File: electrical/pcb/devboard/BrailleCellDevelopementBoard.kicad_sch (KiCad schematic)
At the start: 3 parts, among them J2 USB_C_Receptacle_USB2.0_14P, Q3 PMOS

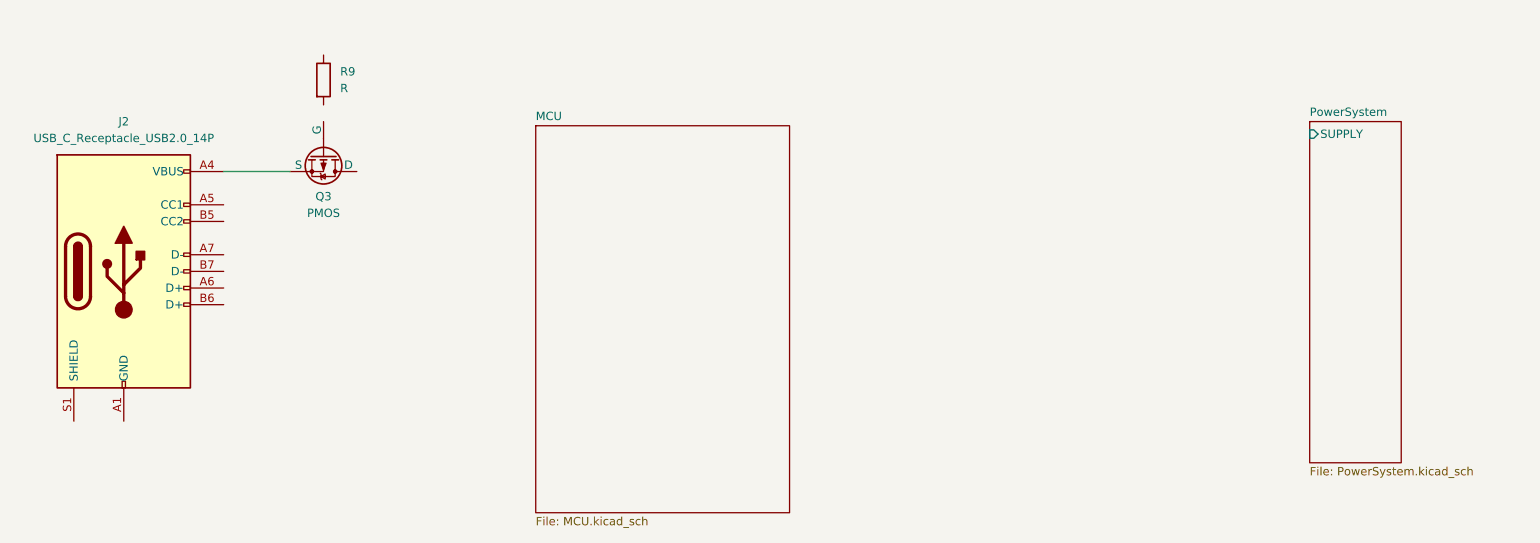
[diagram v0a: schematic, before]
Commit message: cell shifter routed
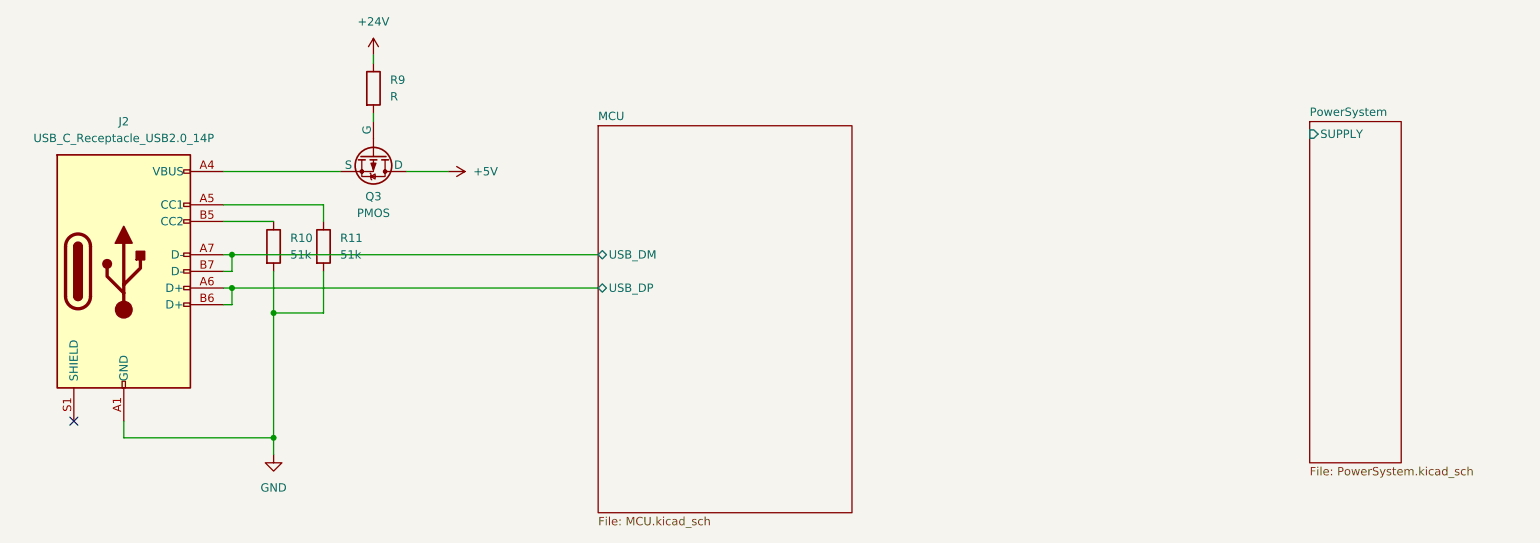
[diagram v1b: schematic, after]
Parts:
- added R10, R11: 51k, symbol Device:R
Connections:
- net +24V: now reaches R9.1
- net at R9.2: now also Q3.2 (G)
- net GND: now reaches J2.A1 (GND), J2.A12 (GND), J2.B1 (GND), J2.B12 (GND)
- net GND: now also R10.2, R11.2
- net at J2.A5 (CC1): now also R11.1
- net MCU/USB_DP: now reaches J2.A6 (D+)
- net MCU/USB_DP: now also J2.B6 (D+)
- net MCU/USB_DM: now reaches J2.A7 (D-)
- net MCU/USB_DM: now also J2.B7 (D-)
- net at J2.B5 (CC2): now also R10.1
- net +5V: now reaches Q3.1 (D)
- no-connect marks 0 -> 1
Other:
- sheet MCU ports: added USB_DM, USB_DP; removed none
- moved on the sheet: Q3, R9

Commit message: Add files via upload
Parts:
- added C15: 10uF, Capacitor_SMD:C_0603_1608Metric, symbol Device:C
- added C16: 0.1uF, Capacitor_SMD:C_0603_1608Metric, symbol Device:C
- J2: footprint (none) -> Connector_USB:USB_C_Receptacle_GCT_USB4085
- Q3: footprint (none) -> Package_SO:SO-8_3.9x4.9mm_P1.27mm
- R10, R11: value 51k -> 5.1k; footprint (none) -> Resistor_SMD:R_0603_1608Metric
- R9: value R -> 100K; footprint (none) -> Resistor_SMD:R_0603_1608Metric
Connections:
- net +5V: now also C16.1
- net GND: now also C15.2, C16.2
- net at J2.A4 (VBUS), J2.A9 (VBUS), J2.B4 (VBUS)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: now also C15.1
